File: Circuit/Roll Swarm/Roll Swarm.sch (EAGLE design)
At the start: 18 parts, among them IC1 MCP1703CB, J7 CORTEX_DEBUG_SMD, U1 MDBT50Q-1MV2, U5 74AHCT2G125

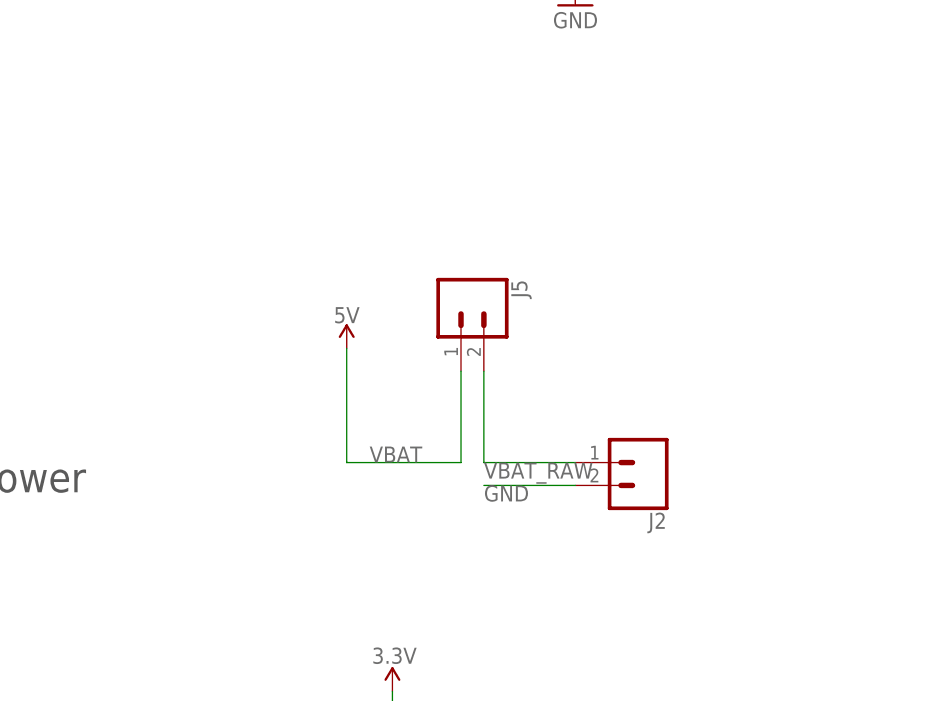
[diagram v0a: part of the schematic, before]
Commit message: Adding new board-mount on/off switch.
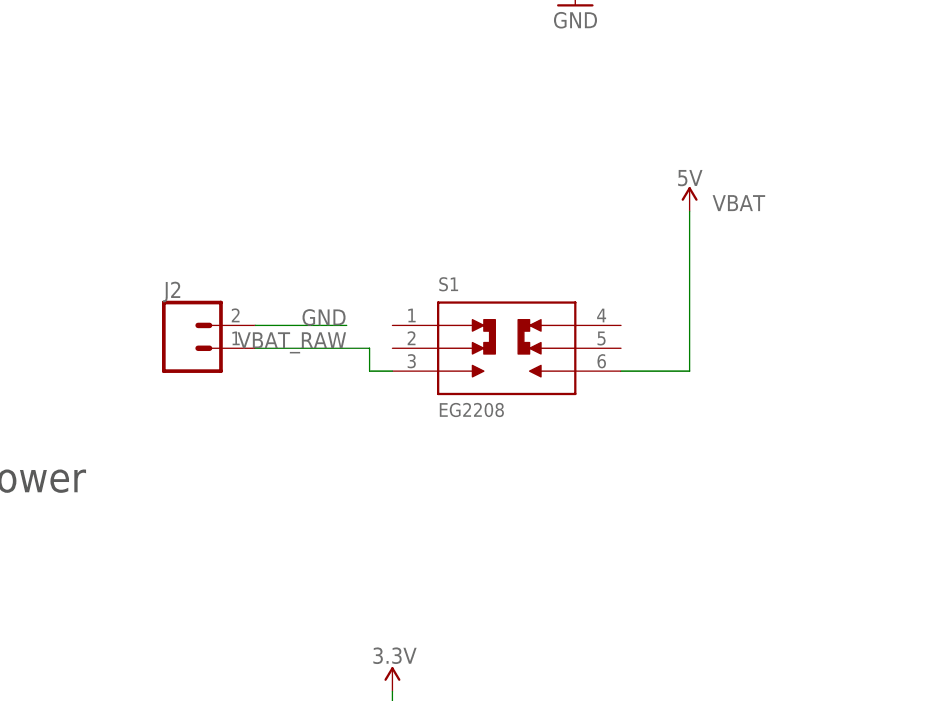
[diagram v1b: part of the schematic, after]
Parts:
- removed J5: (no value), SparkFun-Connectors:CONN_02PTH4
- added S1: EG2208, EG2208:EG2208
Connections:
- net VBAT: now also S1.6; no longer J5.1
- net VBAT_RAW: now also S1.3; no longer J5.2
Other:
- moved on the sheet: J2
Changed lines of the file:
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@@
 <part name="J3" library="SparkFun-Connectors" library_urn="urn:adsk.eagle:library:513" deviceset="CONN_02" device="PTH4" package3d_urn="urn:adsk.eagle:package:38054/1"/>
 <part name="J4" library="SparkFun-Connectors" library_urn="urn:adsk.eagle:library:513" deviceset="CONN_02" device="PTH4" package3d_urn="urn:adsk.eagle:package:38054/1"/>
-<part name="J5" library="SparkFun-Connectors" library_urn="urn:adsk.eagle:library:513" deviceset="CONN_02" device="PTH4" package3d_urn="urn:adsk.eagle:package:38054/1"/>
 <part name="P+1" library="SparkFun-PowerSymbols" deviceset="VCC" device="" value="5V"/>
 <part name="U1" library="MDBT50Q-1MV2" deviceset="MDBT50Q-1MV2" device=""/>
 <part name="GND1" library="SparkFun" deviceset="GND" device=""/>
 <part name="P+4" library="SparkFun" deviceset="3.3V" device="" value="3.3V"/>
+<part name="S1" library="EG2208" deviceset="EG2208" device=""/>
 </parts>
 <sheets>
@@
 <attribute name="DIGIKEY" x="-55.88" y="7.62" size="1.778" layer="96" display="off"/>
 </instance>
-<instance part="J2" gate="G$1" x="-38.1" y="53.34" smashed="yes" rot="R180">
-<attribute name="VALUE" x="-35.56" y="58.166" size="1.778" layer="96" font="vector" rot="R180"/>
-<attribute name="NAME" x="-35.56" y="47.752" size="1.778" layer="95" font="vector" rot="R180"/>
-<attribute name="DIGIKEY" x="-38.1" y="53.34" size="1.778" layer="96" rot="R180" display="off"/>
+<instance part="J2" gate="G$1" x="-88.9" y="66.04" smashed="yes">
+<attribute name="VALUE" x="-91.44" y="61.214" size="1.778" layer="96" font="vector"/>
+<attribute name="NAME" x="-91.44" y="71.628" size="1.778" layer="95" font="vector"/>
+<attribute name="DIGIKEY" x="-88.9" y="66.04" size="1.778" layer="96" display="off"/>
 </instance>
 <instance part="J3" gate="G$1" x="53.34" y="50.8" smashed="yes" rot="R270">
@@
 <attribute name="NAME" x="58.928" y="30.48" size="1.778" layer="95" font="vector" rot="R270"/>
 </instance>
-<instance part="J5" gate="G$1" x="-58.42" y="71.12" smashed="yes" rot="R270">
-<attribute name="VALUE" x="-63.246" y="73.66" size="1.778" layer="96" font="vector" rot="R270"/>
-<attribute name="NAME" x="-52.832" y="73.66" size="1.778" layer="95" font="vector" rot="R270"/>
-</instance>
-<instance part="P+1" gate="G$1" x="-71.12" y="66.04" smashed="yes" rot="MR0">
-<attribute name="VALUE" x="-71.12" y="68.834" size="1.778" layer="96" rot="MR0" align="bottom-center"/>
+<instance part="P+1" gate="G$1" x="-33.02" y="81.28" smashed="yes" rot="MR0">
+<attribute name="VALUE" x="-33.02" y="84.074" size="1.778" layer="96" rot="MR0" align="bottom-center"/>
 </instance>
 <instance part="U1" gate="G$1" x="58.42" y="119.38" smashed="yes">
@@
 <instance part="P+4" gate="G$1" x="104.14" y="167.64" smashed="yes">
 <attribute name="VALUE" x="103.124" y="171.196" size="1.778" layer="96"/>
+</instance>
+<instance part="S1" gate="G$1" x="-53.34" y="66.04" smashed="yes">
+<attribute name="NAME" x="-60.96" y="72.39" size="1.524" layer="95"/>
+<attribute name="VALUE" x="-60.96" y="58.42" size="1.524" layer="96"/>
 </instance>
 </instances>
@@
 <net name="GND" class="0">
 <segment>
-<label x="-55.88" y="50.8" size="1.778" layer="95" rot="MR180"/>
+<label x="-71.12" y="68.58" size="1.778" layer="95" rot="MR0"/>
 <pinref part="J2" gate="G$1" pin="2"/>
-<wire x1="-55.88" y1="50.8" x2="-45.72" y2="50.8" width="0.1524" layer="91"/>
+<wire x1="-71.12" y1="68.58" x2="-81.28" y2="68.58" width="0.1524" layer="91"/>
 </segment>
 <segment>
@@
 <net name="VBAT_RAW" class="0">
 <segment>
-<label x="-55.88" y="53.34" size="1.778" layer="95" rot="MR180"/>
+<label x="-71.12" y="66.04" size="1.778" layer="95" rot="MR0"/>
 <pinref part="J2" gate="G$1" pin="1"/>
-<wire x1="-55.88" y1="53.34" x2="-45.72" y2="53.34" width="0.1524" layer="91"/>
-<pinref part="J5" gate="G$1" pin="2"/>
-<wire x1="-55.88" y1="53.34" x2="-55.88" y2="63.5" width="0.1524" layer="91"/>
+<wire x1="-68.58" y1="66.04" x2="-81.28" y2="66.04" width="0.1524" layer="91"/>
+<wire x1="-68.58" y1="66.04" x2="-68.58" y2="63.5" width="0.1524" layer="91"/>
+<pinref part="S1" gate="G$1" pin="3"/>
+<wire x1="-68.58" y1="63.5" x2="-66.04" y2="63.5" width="0.1524" layer="91"/>
 </segment>
 </net>
@@
 <net name="VBAT" class="0">
 <segment>
-<pinref part="J5" gate="G$1" pin="1"/>
-<wire x1="-58.42" y1="63.5" x2="-58.42" y2="53.34" width="0.1524" layer="91"/>
-<wire x1="-58.42" y1="53.34" x2="-71.12" y2="53.34" width="0.1524" layer="91"/>
-<label x="-68.58" y="53.34" size="1.778" layer="95"/>
-<wire x1="-71.12" y1="53.34" x2="-71.12" y2="66.04" width="0.1524" layer="91"/>
+<label x="-30.48" y="81.28" size="1.778" layer="95"/>
 <pinref part="P+1" gate="G$1" pin="VCC"/>
-</segment>
-<segment>
+<pinref part="S1" gate="G$1" pin="6"/>
+<wire x1="-40.64" y1="63.5" x2="-33.02" y2="63.5" width="0.1524" layer="91"/>
+<wire x1="-33.02" y1="63.5" x2="-33.02" y2="81.28" width="0.1524" layer="91"/>
+</segment>
+<segment>
